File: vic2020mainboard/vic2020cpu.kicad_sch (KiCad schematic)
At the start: 11 parts, among them U3 LM555, U4 7406, U7 W65C02SxP

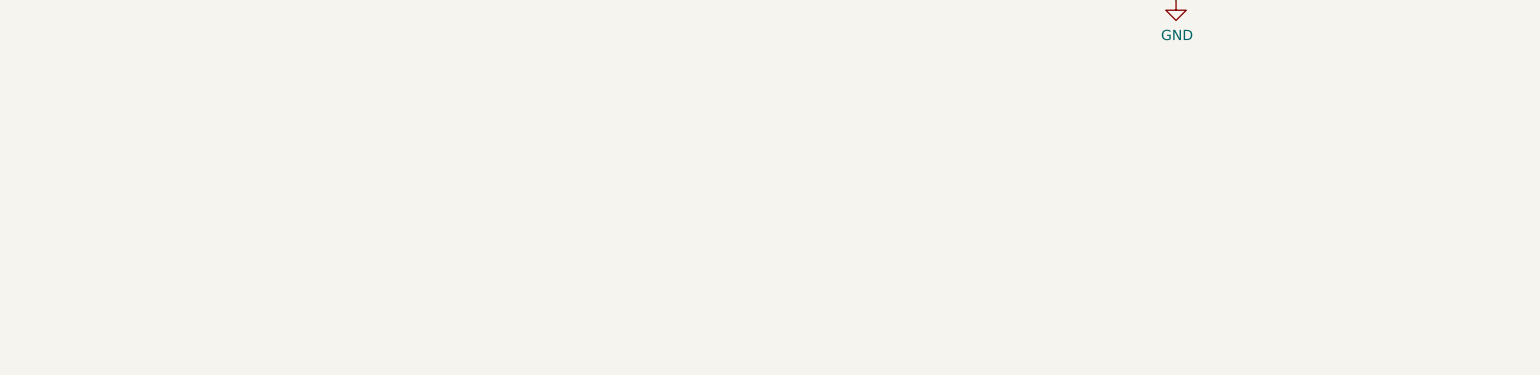
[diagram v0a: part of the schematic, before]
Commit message: Added power supply circuit for 9V AC input
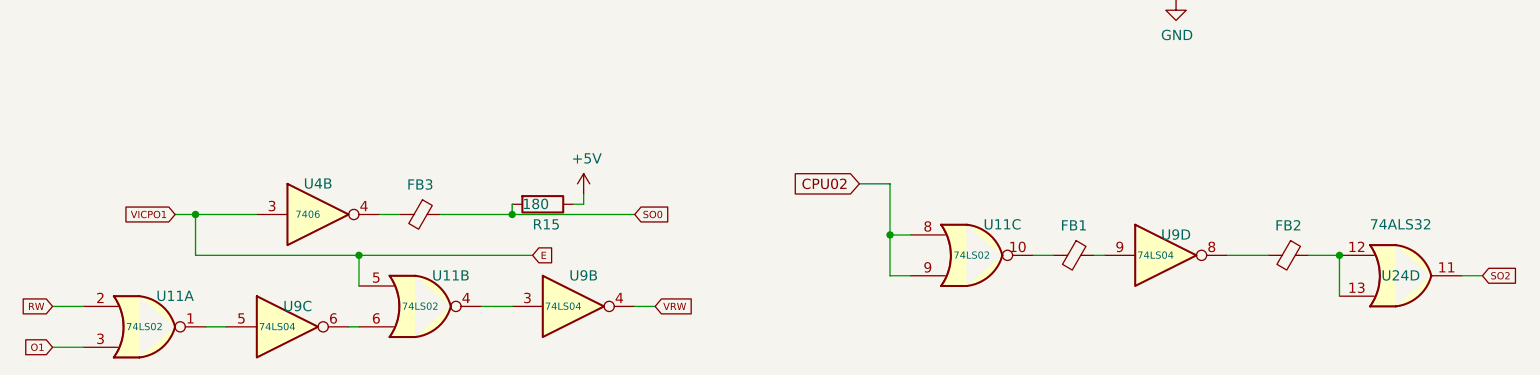
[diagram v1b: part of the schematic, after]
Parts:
- added FB1, FB2, FB3: Ferrite_Bead_Small, Inductor_THT:L_Axial_L6.6mm_D2.7mm_P10.16mm_Horizontal_Vishay_IM-2, symbol Vic2020mainboard-rescue:Ferrite_Bead_Small-Device
- added R15: 180, Resistor_THT:R_Axial_DIN0207_L6.3mm_D2.5mm_P7.62mm_Horizontal, symbol Device:R
- added U11: 74LS02, Package_DIP:DIP-14_W7.62mm_Socket, symbol 74xx:74LS02
- added U24: 74ALS32, Package_DIP:DIP-14_W7.62mm_Socket, symbol 74xx:74LS32
- added unit 2 of U4
- added U9: 74LS04, Package_DIP:DIP-14_W7.62mm_Socket, symbol 74xx:74LS04
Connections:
- net +5V: now also R15.1
- net CPU02: now also U11.8, U11.9
- net O1: now also U11.3
- net RW: now also U11.2
- net SO0: now also FB3.1, R15.2
- new net: U11.1, U9.5
- new net: U11.6, U9.6
- new net: U11.4, U9.3
- new net: FB2.2, U9.8
- new net: FB1.1, U9.9
- new net: FB2.1, U24.12, U24.13
- new net: FB3.2, U4.4
- new net: FB1.2, U11.10
- new net E: U11.5, U4.3
- new net SO2: U24.11
- new net VRW: U9.4
